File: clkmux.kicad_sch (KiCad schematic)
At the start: 10 parts, among them J8 Conn_Coaxial, U4 DS90C401M_NOPB, U5 9DMV0141AKILF

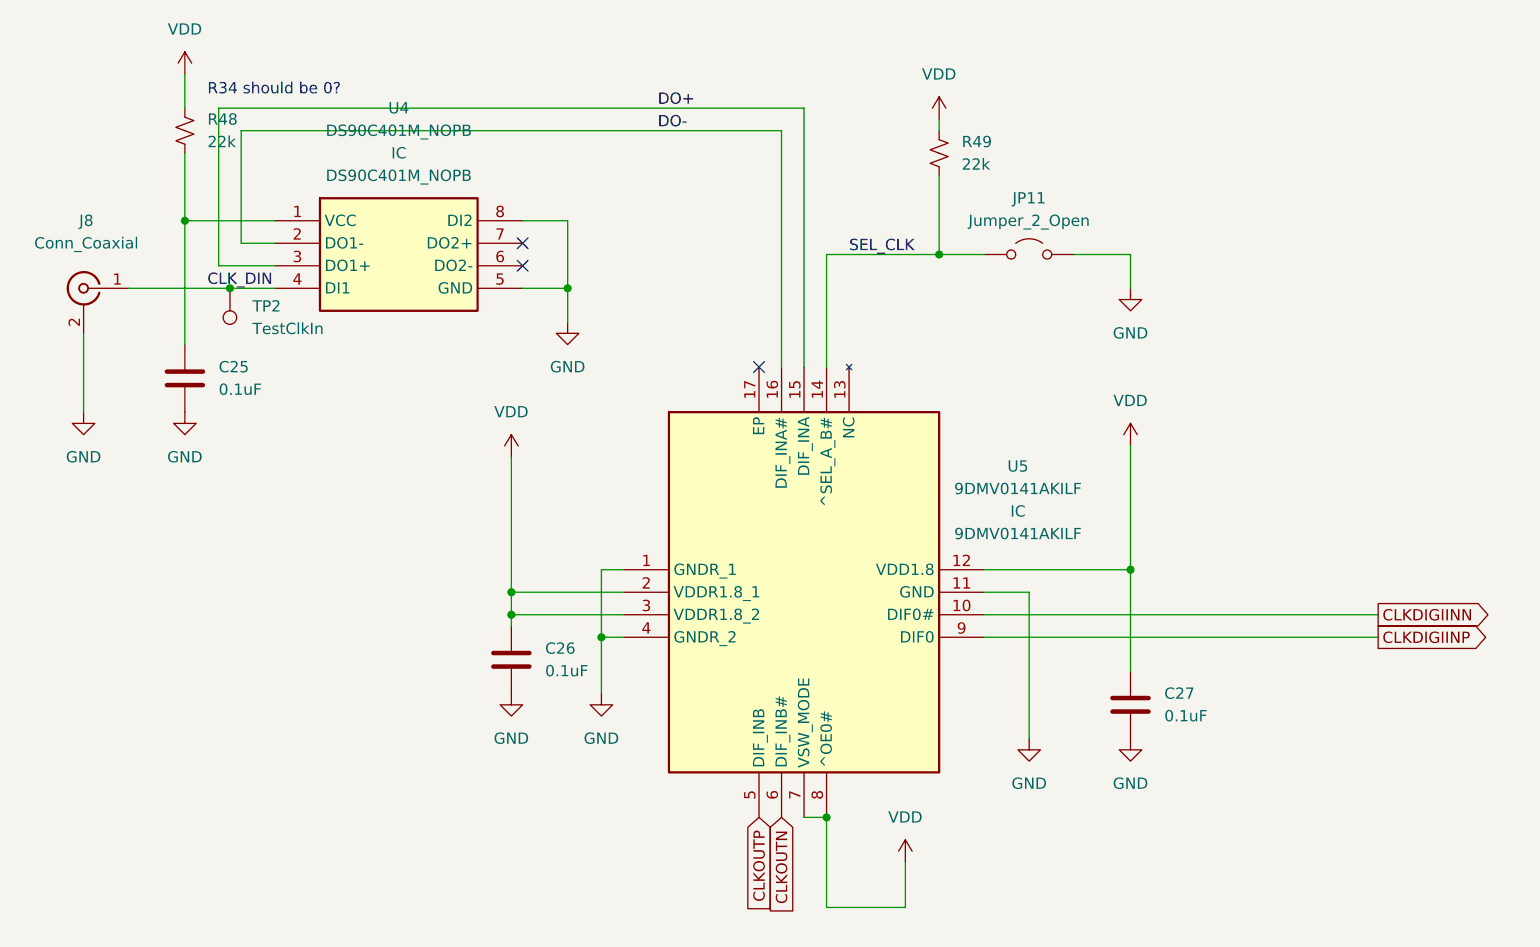
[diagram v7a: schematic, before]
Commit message: add mounting holes, make the board and the zones of rectangular shape, add sikscreen text
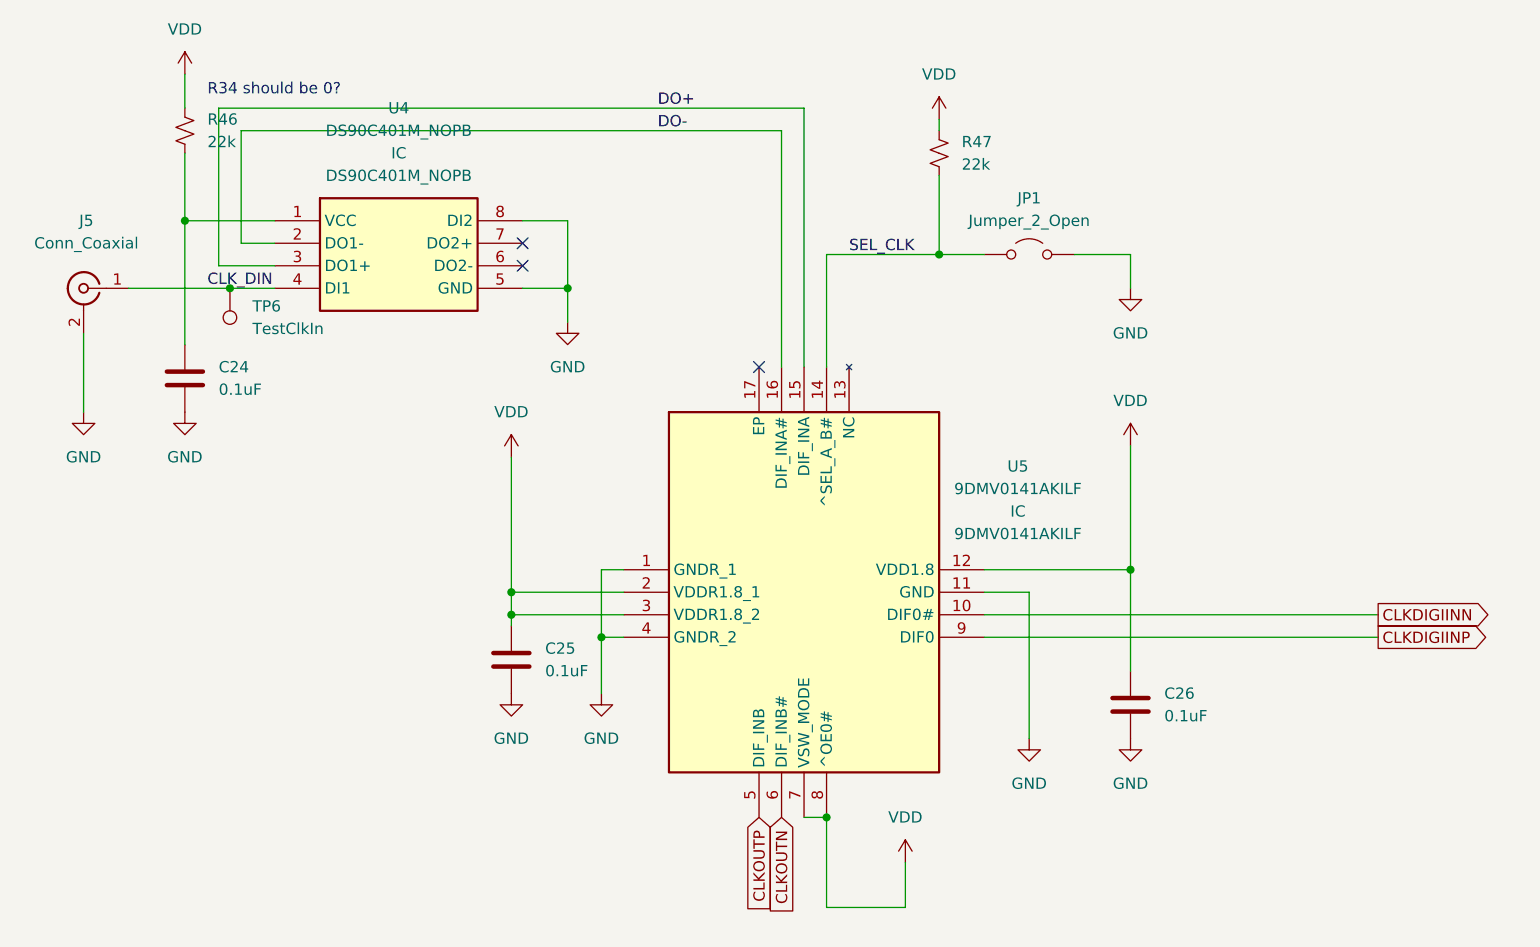
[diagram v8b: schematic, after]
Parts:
- U5: footprint QFN50P300X300X100-17N -> (none)
- renumbered C25 to C24, C26 to C25, C27 to C26, J8 to J5, JP11 to JP1, R48 to R46, R49 to R47, TP2 to TP6
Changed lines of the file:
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@@
 		(dnp no)
 		(fields_autoplaced yes)
-		(property "Reference" "#PWR076"
+		(property "Reference" "#PWR064"
 			(at 59.69 100.33 0)
 			(effects
@@
 			(project "qpix"
 				(path "/68db0a76-6651-4f65-9d5f-4b164c02719b/644af945-7122-4242-b9d9-3e758ef7be8c"
-					(reference "#PWR076")
+					(reference "#PWR064")
 					(unit 1)
 				)
@@
 		(dnp no)
 		(fields_autoplaced yes)
-		(property "Reference" "JP11"
+		(property "Reference" "JP1"
 			(at 166.37 69.85 0)
 			(effects
@@
 			(project "qpix"
 				(path "/68db0a76-6651-4f65-9d5f-4b164c02719b/644af945-7122-4242-b9d9-3e758ef7be8c"
-					(reference "JP11")
+					(reference "JP1")
 					(unit 1)
 				)
@@
 		(on_board yes)
 		(dnp no)
-		(property "Reference" "#PWR083"
+		(property "Reference" "#PWR071"
 			(at 152.4 148.59 0)
 			(effects
@@
 			(project "qpix"
 				(path "/68db0a76-6651-4f65-9d5f-4b164c02719b/644af945-7122-4242-b9d9-3e758ef7be8c"
-					(reference "#PWR083")
+					(reference "#PWR071")
 					(unit 1)
 				)
@@
 		(dnp no)
 		(fields_autoplaced yes)
-		(property "Reference" "#PWR081"
+		(property "Reference" "#PWR069"
 			(at 114.3 90.17 0)
 			(effects
@@
 			(project "qpix"
 				(path "/68db0a76-6651-4f65-9d5f-4b164c02719b/644af945-7122-4242-b9d9-3e758ef7be8c"
-					(reference "#PWR081")
+					(reference "#PWR069")
 					(unit 1)
 				)
@@
 		(on_board yes)
 		(dnp no)
-		(property "Reference" "#PWR084"
+		(property "Reference" "#PWR072"
 			(at 156.21 64.77 0)
 			(effects
@@
 			(project "qpix"
 				(path "/68db0a76-6651-4f65-9d5f-4b164c02719b/644af945-7122-4242-b9d9-3e758ef7be8c"
-					(reference "#PWR084")
+					(reference "#PWR072")
 					(unit 1)
 				)
@@
 		(dnp no)
 		(fields_autoplaced yes)
-		(property "Reference" "#PWR088"
+		(property "Reference" "#PWR076"
 			(at 177.8 137.16 0)
 			(effects
@@
 			(project "qpix"
 				(path "/68db0a76-6651-4f65-9d5f-4b164c02719b/644af945-7122-4242-b9d9-3e758ef7be8c"
-					(reference "#PWR088")
+					(reference "#PWR076")
 					(unit 1)
 				)
@@
 		(dnp no)
 		(fields_autoplaced yes)
-		(property "Reference" "J8"
+		(property "Reference" "J5"
 			(at 60.0074 72.39 0)
 			(effects
@@
 			(project "qpix"
 				(path "/68db0a76-6651-4f65-9d5f-4b164c02719b/644af945-7122-4242-b9d9-3e758ef7be8c"
-					(reference "J8")
+					(reference "J5")
 					(unit 1)
 				)
@@
 		(dnp no)
 		(fields_autoplaced yes)
-		(property "Reference" "#PWR080"
+		(property "Reference" "#PWR068"
 			(at 107.95 132.08 0)
 			(effects
@@
 			(project "qpix"
 				(path "/68db0a76-6651-4f65-9d5f-4b164c02719b/644af945-7122-4242-b9d9-3e758ef7be8c"
-					(reference "#PWR080")
+					(reference "#PWR068")
 					(unit 1)
 				)
@@
 		(dnp no)
 		(fields_autoplaced yes)
-		(property "Reference" "C26"
+		(property "Reference" "C25"
 			(at 111.76 120.65 0)
 			(effects
@@
 			(project "qpix"
 				(path "/68db0a76-6651-4f65-9d5f-4b164c02719b/644af945-7122-4242-b9d9-3e758ef7be8c"
-					(reference "C26")
+					(reference "C25")
 					(unit 1)
 				)
@@
 		(on_board yes)
 		(dnp no)
-		(property "Reference" "#PWR079"
+		(property "Reference" "#PWR067"
 			(at 107.95 102.87 0)
 			(effects
@@
 			(project "qpix"
 				(path "/68db0a76-6651-4f65-9d5f-4b164c02719b/644af945-7122-4242-b9d9-3e758ef7be8c"
-					(reference "#PWR079")
+					(reference "#PWR067")
 					(unit 1)
 				)
@@
 		(dnp no)
 		(fields_autoplaced yes)
-		(property "Reference" "#PWR085"
+		(property "Reference" "#PWR073"
 			(at 166.37 137.16 0)
 			(effects
@@
 			(project "qpix"
 				(path "/68db0a76-6651-4f65-9d5f-4b164c02719b/644af945-7122-4242-b9d9-3e758ef7be8c"
-					(reference "#PWR085")
+					(reference "#PWR073")
 					(unit 1)
 				)
@@
 		(dnp no)
 		(fields_autoplaced yes)
-		(property "Reference" "C25"
+		(property "Reference" "C24"
 			(at 74.93 88.9 0)
 			(effects
@@
 			(project "qpix"
 				(path "/68db0a76-6651-4f65-9d5f-4b164c02719b/644af945-7122-4242-b9d9-3e758ef7be8c"
-					(reference "C25")
+					(reference "C24")
 					(unit 1)
 				)
@@
 		(dnp no)
 		(fields_autoplaced yes)
-		(property "Reference" "#PWR086"
+		(property "Reference" "#PWR074"
 			(at 177.8 86.36 0)
 			(effects
@@
 			(project "qpix"
 				(path "/68db0a76-6651-4f65-9d5f-4b164c02719b/644af945-7122-4242-b9d9-3e758ef7be8c"
-					(reference "#PWR086")
+					(reference "#PWR074")
 					(unit 1)
 				)
@@
 		(on_board yes)
 		(dnp no)
-		(property "Reference" "#PWR087"
+		(property "Reference" "#PWR075"
 			(at 177.8 101.6 0)
 			(effects
@@
 			(project "qpix"
 				(path "/68db0a76-6651-4f65-9d5f-4b164c02719b/644af945-7122-4242-b9d9-3e758ef7be8c"
-					(reference "#PWR087")
+					(reference "#PWR075")
 					(unit 1)
 				)
@@
 		(on_board yes)
 		(dnp no)
-		(property "Reference" "#PWR077"
+		(property "Reference" "#PWR065"
 			(at 71.12 59.69 0)
 			(effects
@@
 			(project "qpix"
 				(path "/68db0a76-6651-4f65-9d5f-4b164c02719b/644af945-7122-4242-b9d9-3e758ef7be8c"
-					(reference "#PWR077")
+					(reference "#PWR065")
 					(unit 1)
 				)
@@
 		(dnp no)
 		(fields_autoplaced yes)
-		(property "Reference" "TP2"
+		(property "Reference" "TP6"
 			(at 78.74 82.0419 0)
 			(effects
@@
 			(project "qpix"
 				(path "/68db0a76-6651-4f65-9d5f-4b164c02719b/644af945-7122-4242-b9d9-3e758ef7be8c"
-					(reference "TP2")
+					(reference "TP6")
 					(unit 1)
 				)
@@
 		(dnp no)
 		(fields_autoplaced yes)
-		(property "Reference" "R49"
+		(property "Reference" "R47"
 			(at 158.75 63.4999 0)
 			(effects
@@
 			(project "qpix"
 				(path "/68db0a76-6651-4f65-9d5f-4b164c02719b/644af945-7122-4242-b9d9-3e758ef7be8c"
-					(reference "R49")
+					(reference "R47")
 					(unit 1)
 				)
@@
 			)
 		)
-		(property "Footprint" "QFN50P300X300X100-17N"
+		(property "Footprint" ""
 			(at 120.65 111.76 0)
 			(effects
@@
 		(dnp no)
 		(fields_autoplaced yes)
-		(property "Reference" "C27"
+		(property "Reference" "C26"
 			(at 181.61 125.7299 0)
 			(effects
@@
 			(project "qpix"
 				(path "/68db0a76-6651-4f65-9d5f-4b164c02719b/644af945-7122-4242-b9d9-3e758ef7be8c"
-					(reference "C27")
+					(reference "C26")
 					(unit 1)
 				)
@@
 		(dnp no)
 		(fields_autoplaced yes)
-		(property "Reference" "R48"
+		(property "Reference" "R46"
 			(at 73.66 60.9599 0)
 			(effects
@@
 			(project "qpix"
 				(path "/68db0a76-6651-4f65-9d5f-4b164c02719b/644af945-7122-4242-b9d9-3e758ef7be8c"
-					(reference "R48")
+					(reference "R46")
 					(unit 1)
 				)
@@
 		(dnp no)
 		(fields_autoplaced yes)
-		(property "Reference" "#PWR082"
+		(property "Reference" "#PWR070"
 			(at 118.11 132.08 0)
 			(effects
@@
 			(project "qpix"
 				(path "/68db0a76-6651-4f65-9d5f-4b164c02719b/644af945-7122-4242-b9d9-3e758ef7be8c"
-					(reference "#PWR082")
+					(reference "#PWR070")
 					(unit 1)
 				)
@@
 		(dnp no)
 		(fields_autoplaced yes)
-		(property "Reference" "#PWR078"
+		(property "Reference" "#PWR066"
 			(at 71.12 100.33 0)
 			(effects
@@
 			(project "qpix"
 				(path "/68db0a76-6651-4f65-9d5f-4b164c02719b/644af945-7122-4242-b9d9-3e758ef7be8c"
-					(reference "#PWR078")
-					(unit 1)
-				)
+					(reference "#PWR066")
+					(unit 1)
+				)
